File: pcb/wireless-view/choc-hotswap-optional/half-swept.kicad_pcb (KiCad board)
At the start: 2 copper layers, 113.3 x 89.7 mm, 26 parts, among them J1 JST-BATTERY, SW1 SW_Push, SW10 SW_Push, SW11 SW_Push, SW12 SW_Push, SW13 SW_DPDT, SW14 SW_Push, SW15 SW_Push, SW16 SW_Push, SW17 SW_Push, SW18 SW_Push, SW2 SW_Push, SW20 SW_Push, SW21 SW_Push, SW3 SW_Push, SW4 SW_Push, SW5 SW_Push, SW6 SW_Push, SW7 SW_DPDT, SW8 SW_Push, SW9 SW_Push, U1 nice_nano

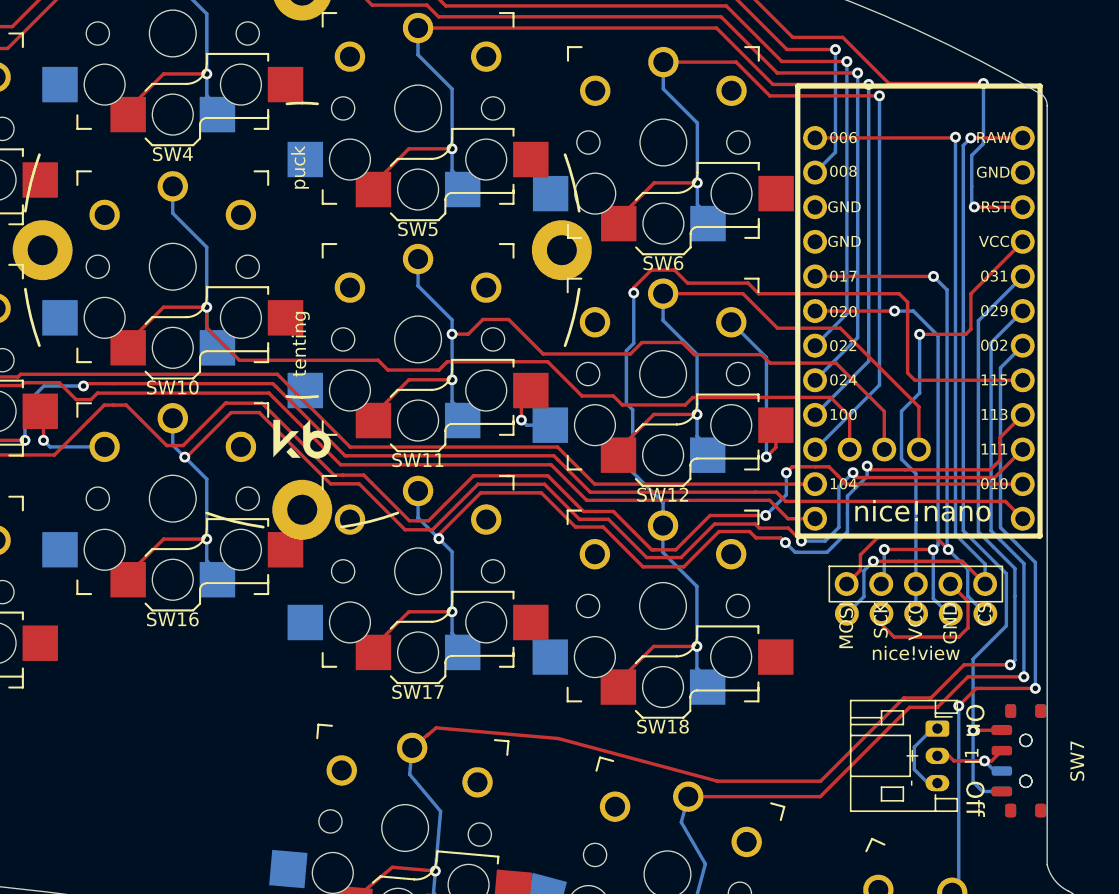
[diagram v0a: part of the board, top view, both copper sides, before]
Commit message: made nice view reversible with jumpers, so it's only one footprint now instead of two offset
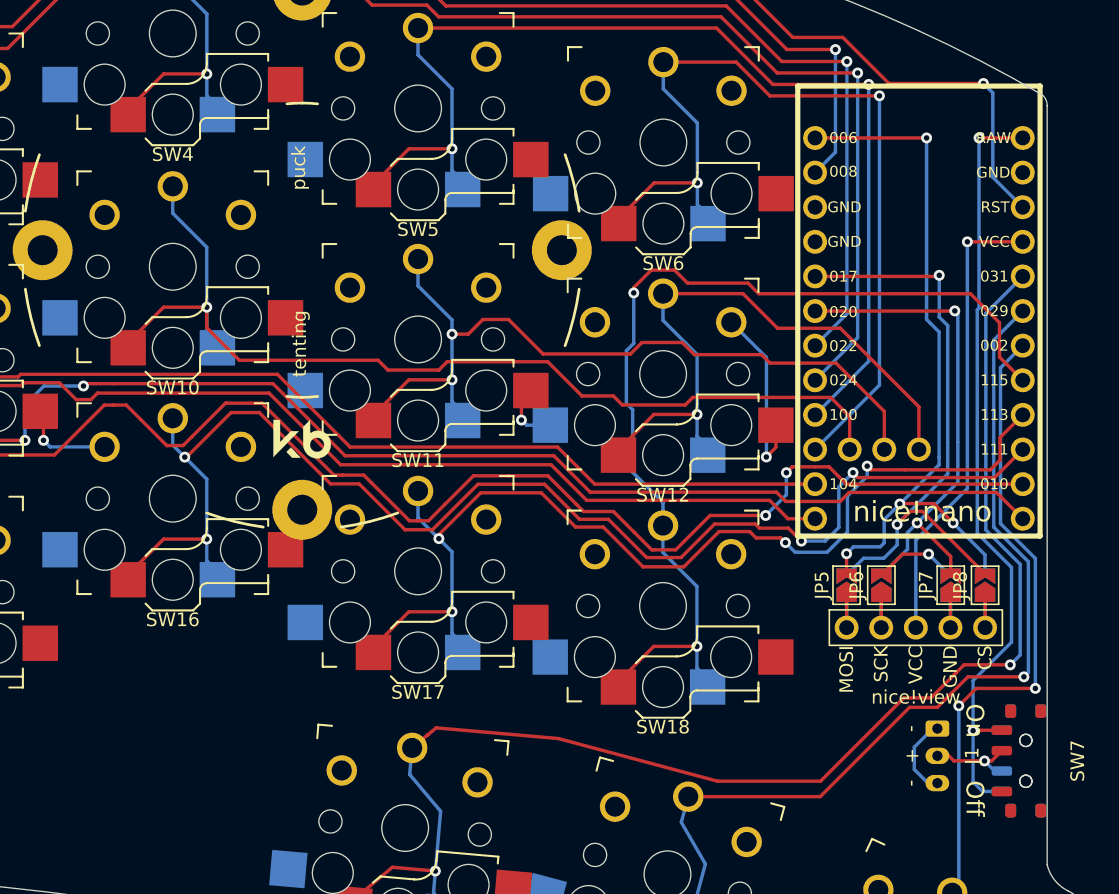
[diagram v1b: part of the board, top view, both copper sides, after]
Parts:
- removed Display2: nice!view, fingerpunch:nice_view
- added JP1: Jumper_2_Open, Jumper:SolderJumper-2_P1.3mm_Open_TrianglePad1.0x1.5mm, B.Cu at (118.2, 62.8)
- added JP2: Jumper_2_Open, Jumper:SolderJumper-2_P1.3mm_Open_TrianglePad1.0x1.5mm, B.Cu at (115.7, 62.8)
- added JP3: Jumper_2_Open, Jumper:SolderJumper-2_P1.3mm_Open_TrianglePad1.0x1.5mm, B.Cu at (110.6, 62.8)
- added JP4: Jumper_2_Open, Jumper:SolderJumper-2_P1.3mm_Open_TrianglePad1.0x1.5mm, B.Cu at (108.1, 62.8)
- added JP5: Jumper_2_Open, Jumper:SolderJumper-2_P1.3mm_Open_TrianglePad1.0x1.5mm, F.Cu at (108.1, 62.8)
- added JP6: Jumper_2_Open, Jumper:SolderJumper-2_P1.3mm_Open_TrianglePad1.0x1.5mm, F.Cu at (110.6, 62.8)
- added JP7: Jumper_2_Open, Jumper:SolderJumper-2_P1.3mm_Open_TrianglePad1.0x1.5mm, F.Cu at (115.7, 62.8)
- added JP8: Jumper_2_Open, Jumper:SolderJumper-2_P1.3mm_Open_TrianglePad1.0x1.5mm, F.Cu at (118.2, 62.8)
- moved Display1 3.20 mm to (113.2, 49.4)
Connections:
- Display1 pad 1: mosi -> Net-(Display1-Pad1)
- Display1 pad 2: sck -> Net-(Display1-Pad2)
- Display1 pad 4: gnd -> Net-(Display1-Pad4)
- Display1 pad 5: nv_cs -> Net-(Display1-Pad5)
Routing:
- net gnd: track 36.8 -> 31.6 mm, vias 3 -> 4
- net Net-(Display1-Pad4): track 0.00 -> 4.79 mm
- net Net-(Display1-Pad2): track 0.00 -> 4.78 mm
- net Net-(Display1-Pad1): track 0.00 -> 4.78 mm
- net Net-(Display1-Pad5): track 0.00 -> 4.78 mm
- net nv_cs: track 57.6 -> 53.9 mm, vias 2 -> 4
- net reset: track 57.4 -> 54.6 mm, vias 2 -> 1
- net Switch15: track 74.7 -> 73.1 mm
- net raw: track 58.1 -> 57.2 mm
- net mosi: track 44.9 -> 44.2 mm
- net vcc: track 33.4 -> 33.9 mm
- net Switch11: track 149.0 -> 149.5 mm
- net sck: track 37.2 -> 36.9 mm, vias 3 -> 2

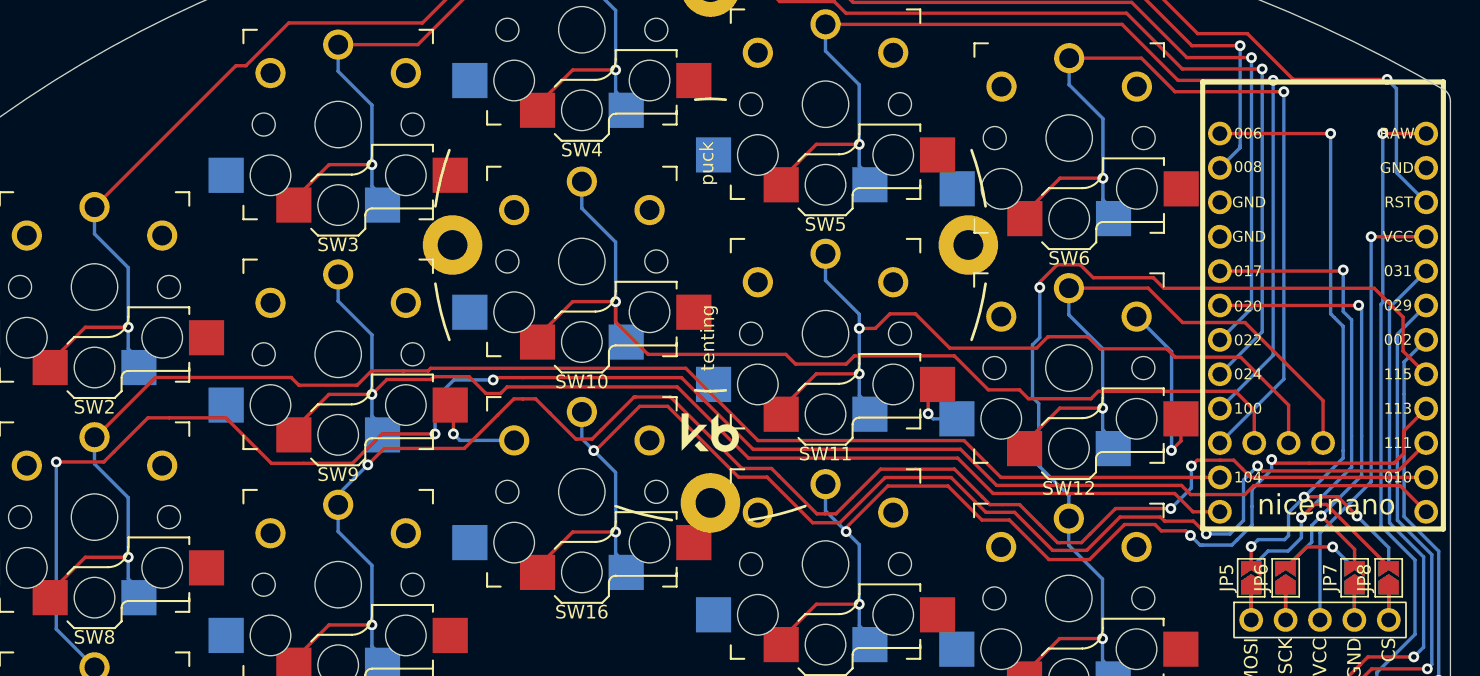
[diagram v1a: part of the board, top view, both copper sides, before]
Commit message: added fingerpunch logo
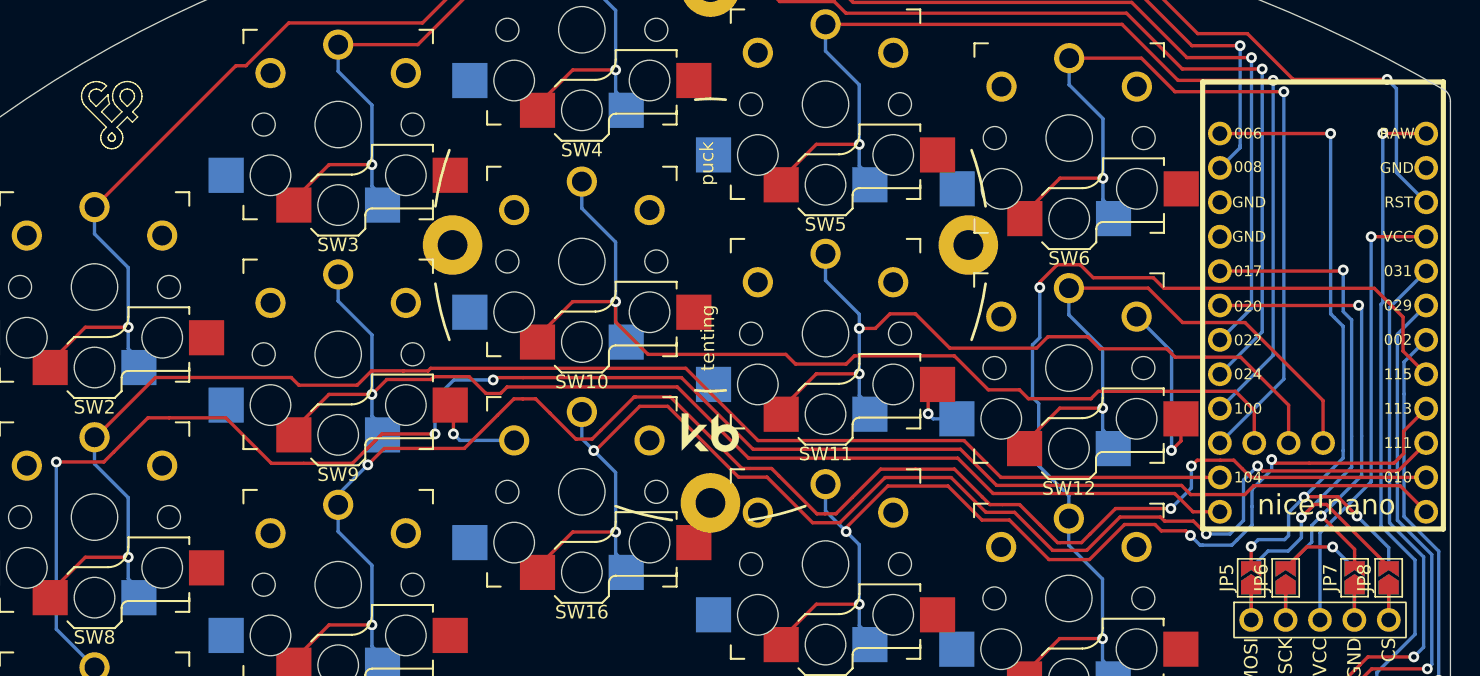
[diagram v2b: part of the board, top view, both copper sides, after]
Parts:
- added REF**: fingerpunch-logo-small, fingerpunch:fingerpunch-logo-small, F.Cu at (23.9, 28.4)
- added REF**: fingerpunch-logo-small, fingerpunch:fingerpunch-logo-small, B.Cu at (23.9, 28.4)
